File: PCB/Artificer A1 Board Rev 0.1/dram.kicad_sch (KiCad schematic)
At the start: 1 part, among them U4 K4F6E3S4HM-MGCJ

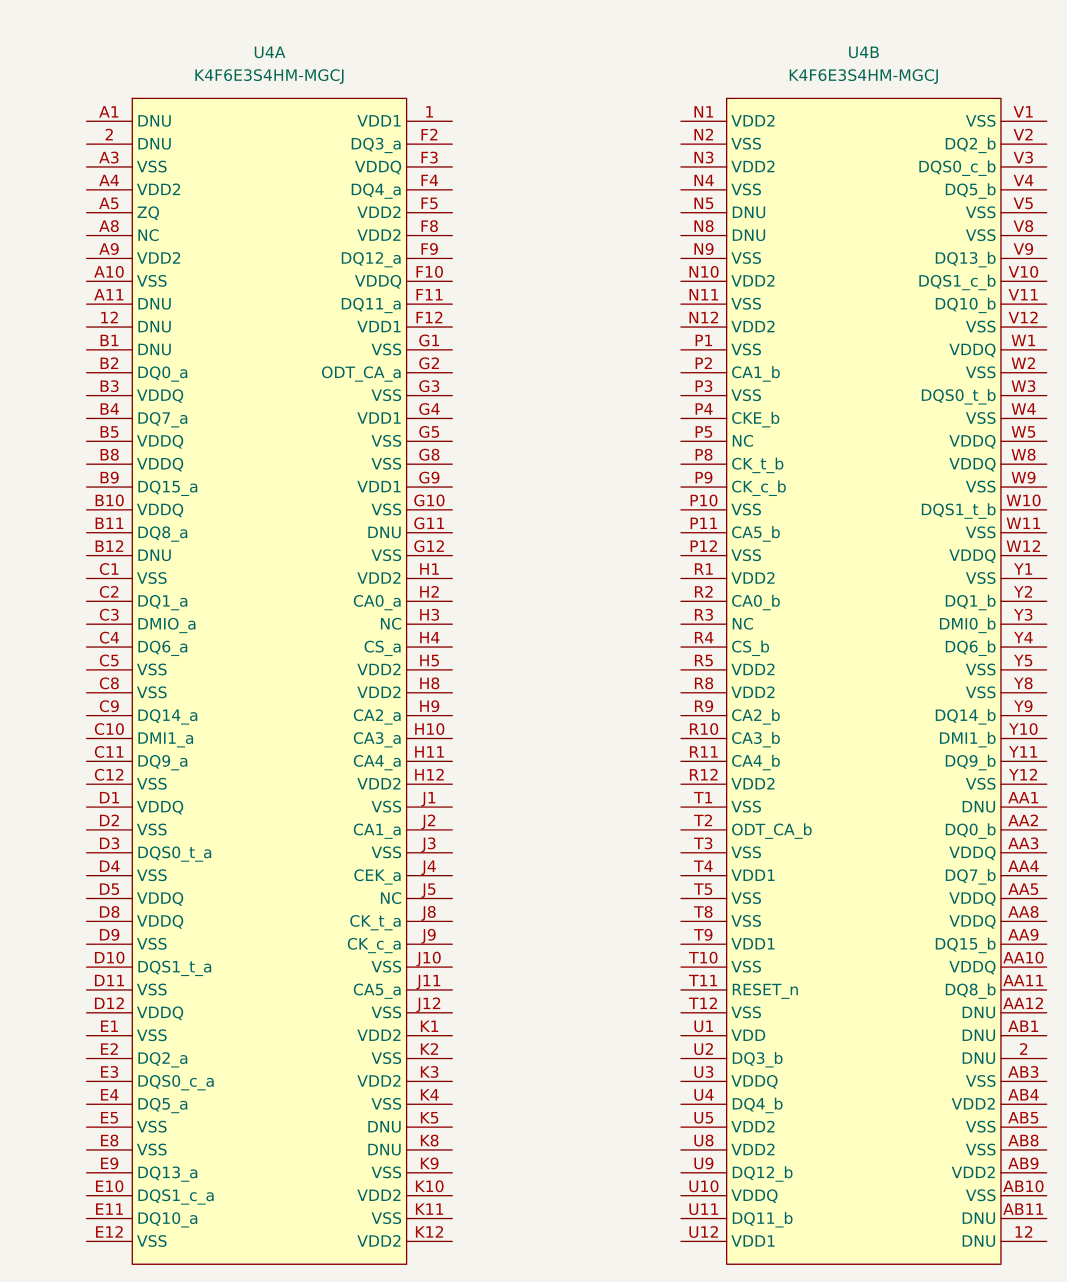
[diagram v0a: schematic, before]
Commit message: localized libraries
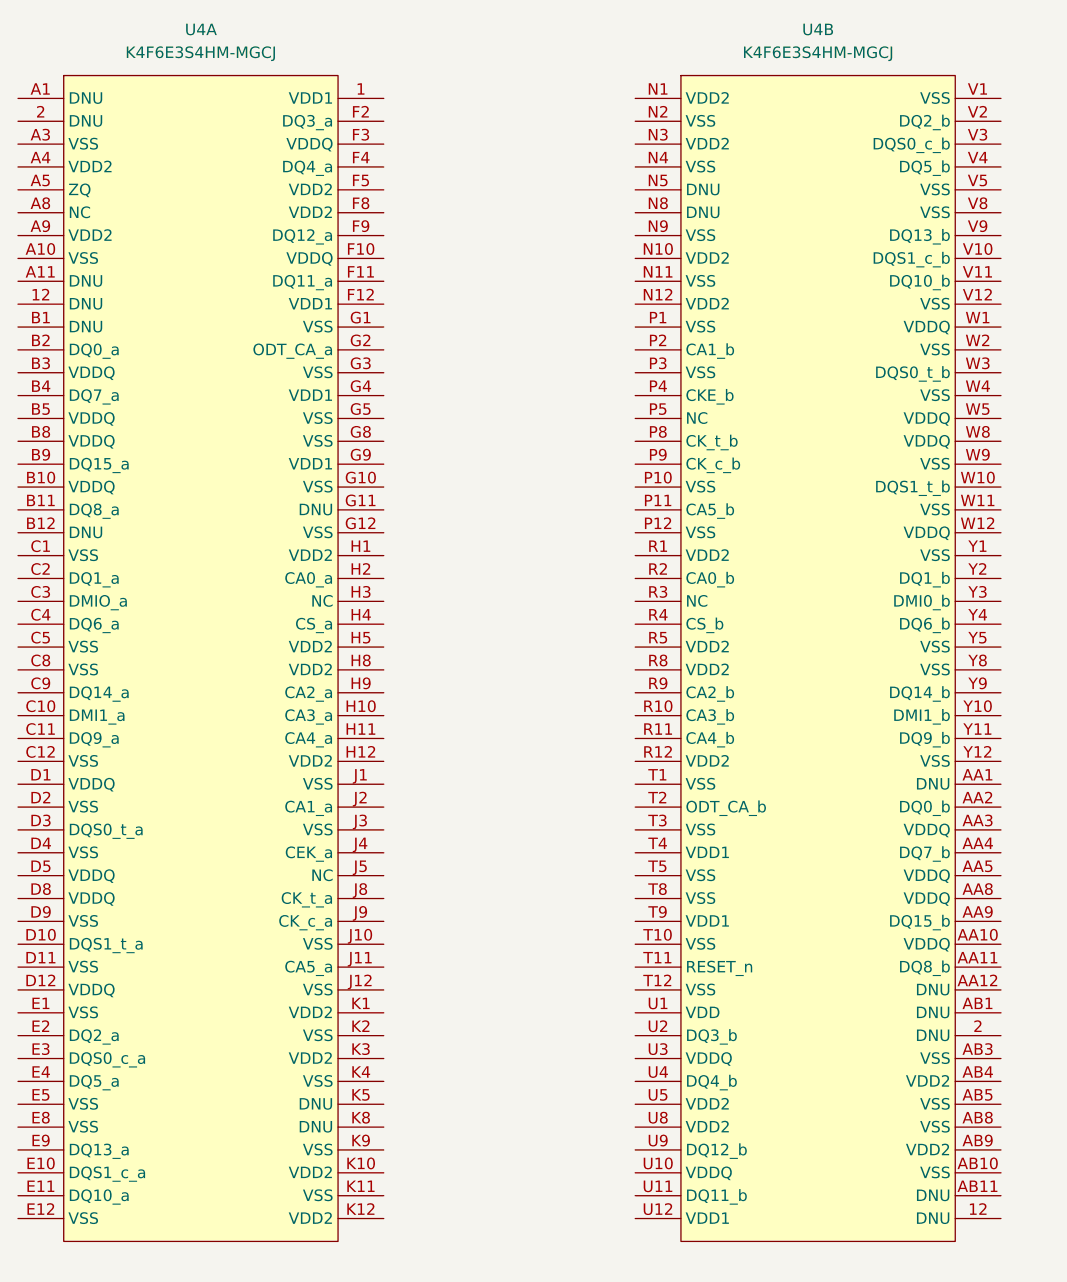
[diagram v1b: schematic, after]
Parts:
- removed U4: K4F6E3S4HM-MGCJ, easyeda2kicad:FBGA-200_L15.0-W10.0-BL_K4F6E3S4HM, symbol easyeda2kicad:K4F6E3S4HM-MGCJ
- added U4: K4F6E3S4HM-MGCJ, easyeda:FBGA-200_L15.0-W10.0-BL_K4F6E3S4HM, symbol easyeda:K4F6E3S4HM-MGCJ

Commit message: added a few accessories
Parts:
- removed U4: K4F6E3S4HM-MGCJ, easyeda:FBGA-200_L15.0-W10.0-BL_K4F6E3S4HM, symbol easyeda:K4F6E3S4HM-MGCJ
- added U14: K4UBE3D4AB-MGCL, easyeda:FBGA-200_L14.5-W10.0_RS1G32LF4D2BDS-53BT, symbol easyeda:K4UBE3D4AB-MGCL

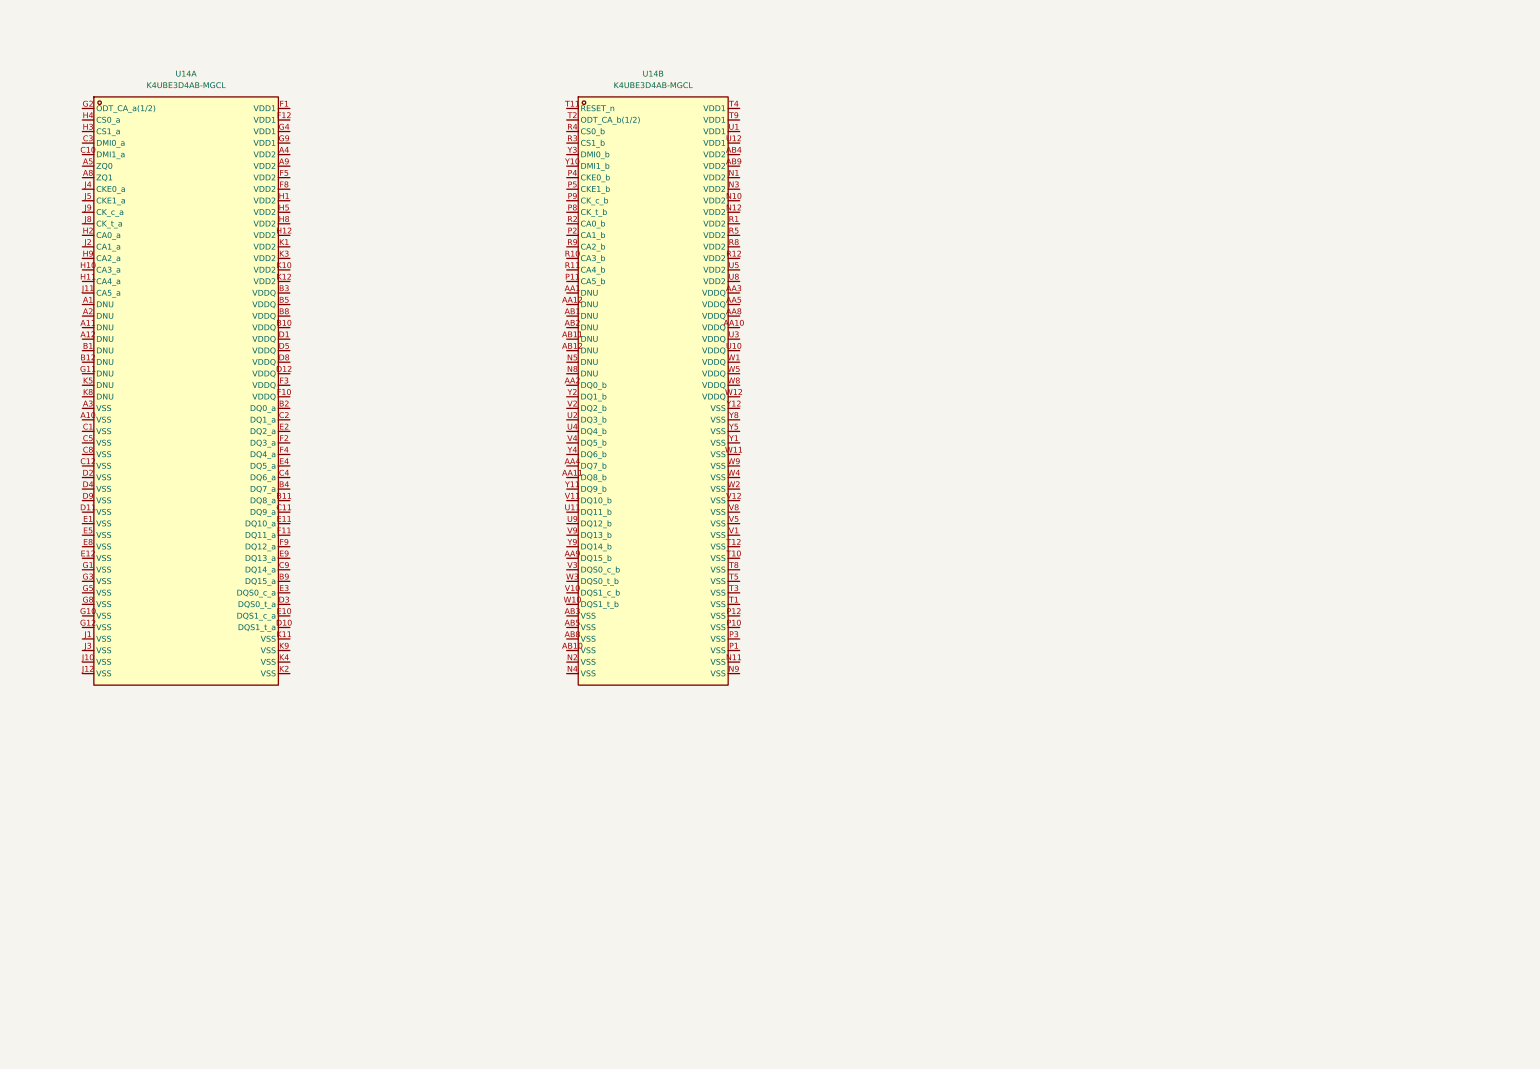
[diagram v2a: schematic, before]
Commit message: finished dram
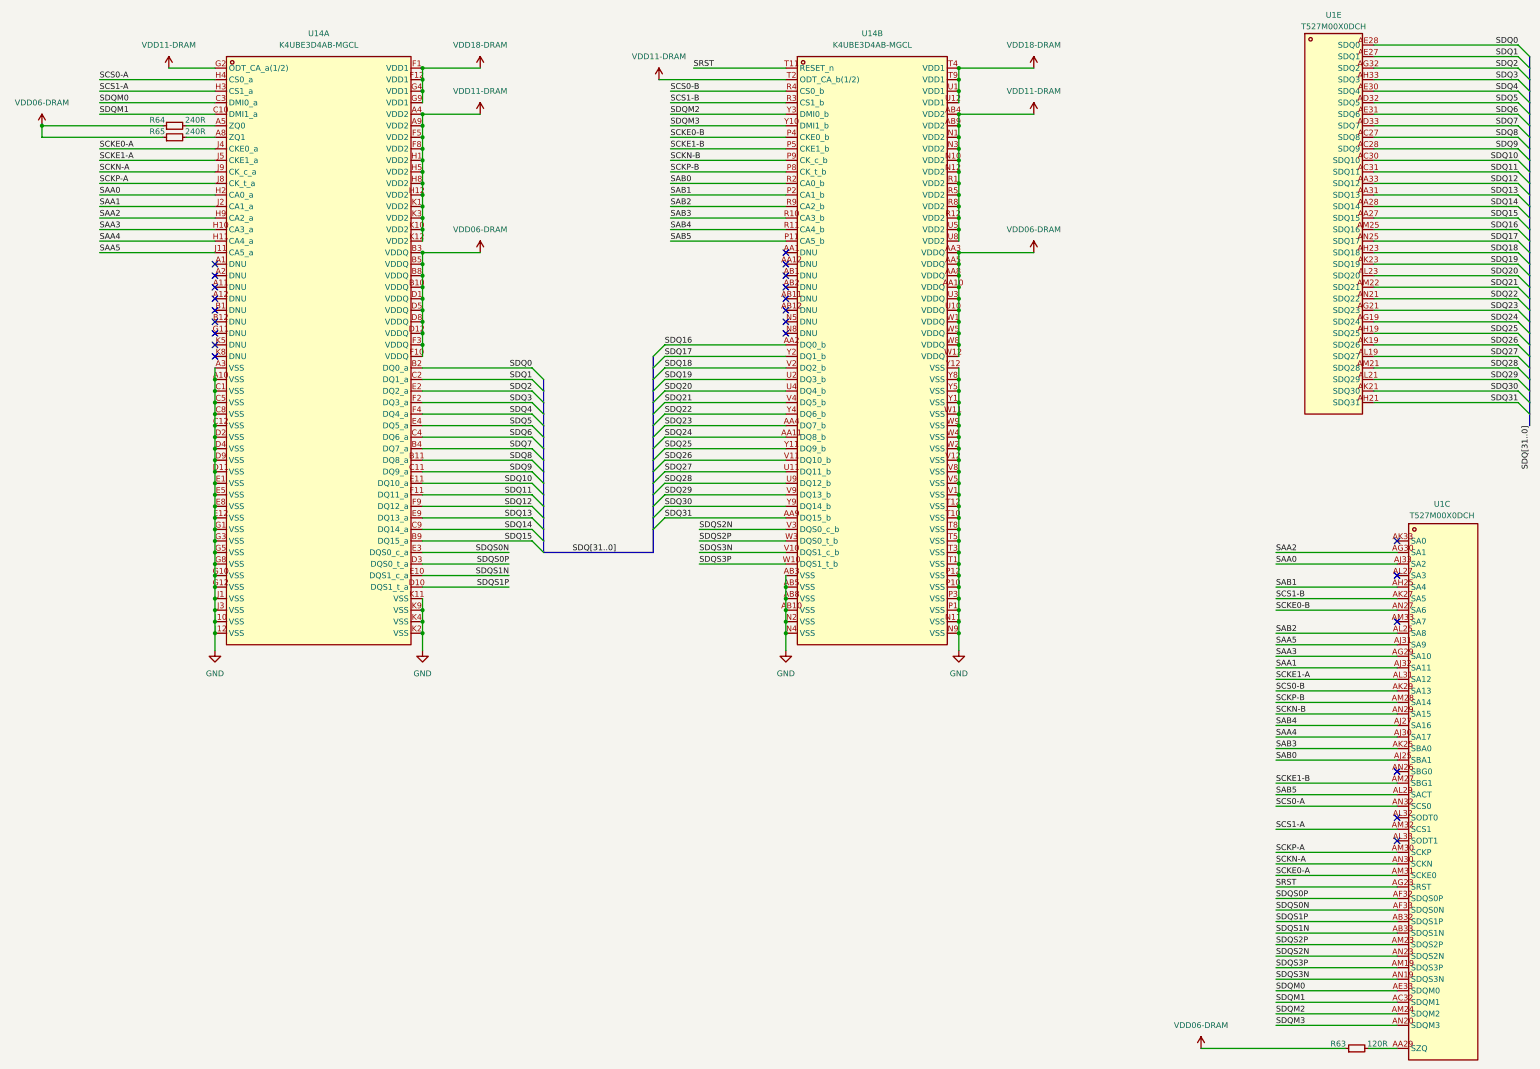
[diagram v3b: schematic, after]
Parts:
- added R63: 120R, symbol Device:R_Small
- added R64, R65: 240R, symbol Device:R_Small
- added U1: T527M00X0DCH, easyeda:BGA-664_L17.0-W17.0_T527, symbol easyeda:T527M00X0DCH
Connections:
- net GND: now reaches U14.A10 (VSS)
- net GND: now also U14.A3 (VSS), U14.AB10 (VSS), U14.AB3 (VSS), U14.AB5 (VSS), U14.AB8 (VSS), U14.C1 (VSS), U14.C12 (VSS), U14.C5 (VSS), U14.C8 (VSS), U14.D11 (VSS), U14.D2 (VSS), U14.D4 (VSS), U14.D9 (VSS), U14.E1 (VSS), U14.E12 (VSS), U14.E5 (VSS), U14.E8 (VSS), U14.G1 (VSS), U14.G10 (VSS), U14.G12 (VSS), U14.G3 (VSS), U14.G5 (VSS), U14.G8 (VSS), U14.J1 (VSS), U14.J10 (VSS), U14.J12 (VSS), U14.J3 (VSS), U14.K11 (VSS), U14.K2 (VSS), U14.K4 (VSS), U14.K9 (VSS), U14.N11 (VSS), U14.N2 (VSS), U14.N4 (VSS), U14.N9 (VSS), U14.P1 (VSS), U14.P10 (VSS), U14.P12 (VSS), U14.P3 (VSS), U14.T1 (VSS), U14.T10 (VSS), U14.T12 (VSS), U14.T3 (VSS), U14.T5 (VSS), U14.T8 (VSS), U14.V1 (VSS), U14.V12 (VSS), U14.V5 (VSS), U14.V8 (VSS), U14.W11 (VSS), U14.W2 (VSS), U14.W4 (VSS), U14.W9 (VSS), U14.Y1 (VSS), U14.Y12 (VSS), U14.Y5 (VSS), U14.Y8 (VSS)
- net VDD11-DRAM: now reaches U14.A4 (VDD2)
- net VDD11-DRAM: now also U14.A9 (VDD2), U14.AB4 (VDD2), U14.AB9 (VDD2), U14.F5 (VDD2), U14.F8 (VDD2), U14.G2 (ODT_CA_a(1/2)), U14.H1 (VDD2), U14.H12 (VDD2), U14.H5 (VDD2), U14.H8 (VDD2), U14.K1 (VDD2), U14.K10 (VDD2), U14.K12 (VDD2), U14.K3 (VDD2), U14.N1 (VDD2), U14.N10 (VDD2), U14.N12 (VDD2), U14.N3 (VDD2), U14.R1 (VDD2), U14.R12 (VDD2), U14.R5 (VDD2), U14.R8 (VDD2), U14.T2 (ODT_CA_b(1/2)), U14.U5 (VDD2), U14.U8 (VDD2)
- net at U14.A5 (ZQ0): now also R64.2
- net at U14.A8 (ZQ1): now also R65.2
- net VDD06-DRAM: now reaches U14.B10 (VDDQ)
- net VDD06-DRAM: now also U14.AA10 (VDDQ), U14.AA3 (VDDQ), U14.AA5 (VDDQ), U14.AA8 (VDDQ), U14.B3 (VDDQ), U14.B5 (VDDQ), U14.B8 (VDDQ), U14.D1 (VDDQ), U14.D12 (VDDQ), U14.D5 (VDDQ), U14.D8 (VDDQ), U14.F10 (VDDQ), U14.F3 (VDDQ), U14.U10 (VDDQ), U14.U3 (VDDQ), U14.W1 (VDDQ), U14.W12 (VDDQ), U14.W5 (VDDQ), U14.W8 (VDDQ), R63.1, R64.1, R65.1
- net SDQ8: now reaches U14.B11 (DQ8_a)
- net SDQ8: now also U1.AC27 (SDQ8)
- net SDQ0: now reaches U14.B2 (DQ0_a)
- net SDQ0: now also U1.AE28 (SDQ0)
- net SDQ7: now reaches U14.B4 (DQ7_a)
- net SDQ7: now also U1.AD33 (SDQ7)
- net SDQ15: now reaches U14.B9 (DQ15_a)
- net SDQ15: now also U1.AA27 (SDQ15)
- net SDQM1: now reaches U14.C10 (DMI1_a)
- net SDQM1: now also U1.AC32 (SDQM1)
- net SDQ9: now reaches U14.C11 (DQ9_a)
- net SDQ9: now also U1.AC28 (SDQ9)
- net SDQ1: now reaches U14.C2 (DQ1_a)
- net SDQ1: now also U1.AE27 (SDQ1)
- net SDQM0: now reaches U14.C3 (DMI0_a)
- net SDQM0: now also U1.AE33 (SDQM0)
- net SDQ6: now reaches U14.C4 (DQ6_a)
- net SDQ6: now also U1.AE31 (SDQ6)
- net SDQ14: now reaches U14.C9 (DQ14_a)
- net SDQ14: now also U1.AA28 (SDQ14)
- net SDQS1P: now reaches U14.D10 (DQS1_t_a)
- net SDQS1P: now also U1.AB32 (SDQS1P)
- net SDQS0P: now reaches U14.D3 (DQS0_t_a)
- net SDQS0P: now also U1.AF32 (SDQS0P)
- net SDQS1N: now reaches U14.E10 (DQS1_c_a)
- net SDQS1N: now also U1.AB33 (SDQS1N)
- net SDQ10: now reaches U14.E11 (DQ10_a)
- net SDQ10: now also U1.AC30 (SDQ10)
- net SDQ2: now reaches U14.E2 (DQ2_a)
- net SDQ2: now also U1.AG32 (SDQ2)
- net SDQS0N: now reaches U14.E3 (DQS0_c_a)
- net SDQS0N: now also U1.AF33 (SDQS0N)
- net SDQ5: now reaches U14.E4 (DQ5_a)
- net SDQ5: now also U1.AD32 (SDQ5)
- net SDQ13: now reaches U14.E9 (DQ13_a)
- net SDQ13: now also U1.AA31 (SDQ13)
- net VDD18-DRAM: now reaches U14.F1 (VDD1)
- net VDD18-DRAM: now also U14.F12 (VDD1), U14.G4 (VDD1), U14.G9 (VDD1), U14.T4 (VDD1), U14.T9 (VDD1), U14.U1 (VDD1), U14.U12 (VDD1)
- net SDQ11: now reaches U14.F11 (DQ11_a)
- net SDQ11: now also U1.AC31 (SDQ11)
- net SDQ3: now reaches U14.F2 (DQ3_a)
- net SDQ3: now also U1.AH33 (SDQ3)
- net SDQ4: now reaches U14.F4 (DQ4_a)
- net SDQ4: now also U1.AE30 (SDQ4)
- net SDQ12: now reaches U14.F9 (DQ12_a)
- net SDQ12: now also U1.AA33 (SDQ12)
- net SAA3: now reaches U14.H10 (CA3_a)
- net SAA3: now also U1.AG29 (SA10)
- net SAA4: now reaches U14.H11 (CA4_a)
- net SAA4: now also U1.AJ30 (SA17)
- net SAA0: now reaches U14.H2 (CA0_a)
- net SAA0: now also U1.AJ33 (SA2)
- net SCS1-A: now reaches U14.H3 (CS1_a)
- net SCS1-A: now also U1.AM32 (SCS1)
- net SCS0-A: now reaches U14.H4 (CS0_a)
- net SCS0-A: now also U1.AN32 (SCS0)
- net SAA2: now reaches U14.H9 (CA2_a)
- net SAA2: now also U1.AG30 (SA1)
- net SAA5: now reaches U14.J11 (CA5_a)
- net SAA5: now also U1.AJ31 (SA9)
- net SAA1: now reaches U14.J2 (CA1_a)
- net SAA1: now also U1.AJ32 (SA11)
- net SCKE0-A: now reaches U14.J4 (CKE0_a)
- net SCKE0-A: now also U1.AM31 (SCKE0)
- net SCKE1-A: now reaches U14.J5 (CKE1_a)
- net SCKE1-A: now also U1.AL31 (SA12)
- net SCKP-A: now reaches U14.J8 (CK_t_a)
- net SCKP-A: now also U1.AM30 (SCKP)
- net SCKN-A: now reaches U14.J9 (CK_c_a)
- net SCKN-A: now also U1.AN30 (SCKN)
- net SDQ24: now reaches U14.AA11 (DQ8_b)
- net SDQ24: now also U1.AG19 (SDQ24)
- net SDQ16: now reaches U14.AA2 (DQ0_b)
- net SDQ16: now also U1.AM25 (SDQ16)
- net SDQ23: now reaches U14.AA4 (DQ7_b)
- net SDQ23: now also U1.AG21 (SDQ23)
- net SDQ31: now reaches U14.AA9 (DQ15_b)
- net SDQ31: now also U1.AH21 (SDQ31)
- net SAB5: now reaches U14.P11 (CA5_b)
- net SAB5: now also U1.AL29 (SACT)
- net SAB1: now reaches U14.P2 (CA1_b)
- net SAB1: now also U1.AH25 (SA4)
- net SCKE0-B: now reaches U14.P4 (CKE0_b)
- net SCKE0-B: now also U1.AN27 (SA6)
- net SCKE1-B: now reaches U14.P5 (CKE1_b)
- net SCKE1-B: now also U1.AM27 (SBG1)
- net SCKP-B: now reaches U14.P8 (CK_t_b)
- net SCKP-B: now also U1.AM28 (SA14)
- net SCKN-B: now reaches U14.P9 (CK_c_b)
- net SCKN-B: now also U1.AN29 (SA15)
- net SAB3: now reaches U14.R10 (CA3_b)
- net SAB3: now also U1.AK25 (SBA0)
- net SAB4: now reaches U14.R11 (CA4_b)
- net SAB4: now also U1.AJ27 (SA16)
- net SAB0: now reaches U14.R2 (CA0_b)
- net SAB0: now also U1.AJ25 (SBA1)
- net SCS1-B: now reaches U14.R3 (CS1_b)
- net SCS1-B: now also U1.AK27 (SA5)
- net SCS0-B: now reaches U14.R4 (CS0_b)
- net SCS0-B: now also U1.AK29 (SA13)
- net SAB2: now reaches U14.R9 (CA2_b)
- net SAB2: now also U1.AL25 (SA8)
- net SRST: now reaches U14.T11 (RESET_n)
- net SRST: now also U1.AG23 (SRST)
- net SDQ27: now reaches U14.U11 (DQ11_b)
- net SDQ27: now also U1.AL19 (SDQ27)
- net SDQ19: now reaches U14.U2 (DQ3_b)
- net SDQ19: now also U1.AK23 (SDQ19)
- net SDQ20: now reaches U14.U4 (DQ4_b)
- net SDQ20: now also U1.AL23 (SDQ20)
- net SDQ28: now reaches U14.U9 (DQ12_b)
- net SDQ28: now also U1.AM21 (SDQ28)
- net SDQS3N: now reaches U14.V10 (DQS1_c_b)
- net SDQS3N: now also U1.AN19 (SDQS3N)
- net SDQ26: now reaches U14.V11 (DQ10_b)
- net SDQ26: now also U1.AK19 (SDQ26)
- net SDQ18: now reaches U14.V2 (DQ2_b)
- net SDQ18: now also U1.AH23 (SDQ18)
- net SDQS2N: now reaches U14.V3 (DQS0_c_b)
- net SDQS2N: now also U1.AN23 (SDQS2N)
- net SDQ21: now reaches U14.V4 (DQ5_b)
- net SDQ21: now also U1.AM22 (SDQ21)
- net SDQ29: now reaches U14.V9 (DQ13_b)
- net SDQ29: now also U1.AL21 (SDQ29)
- net SDQS3P: now reaches U14.W10 (DQS1_t_b)
- net SDQS3P: now also U1.AM19 (SDQS3P)
- net SDQS2P: now reaches U14.W3 (DQS0_t_b)
- net SDQS2P: now also U1.AM23 (SDQS2P)
- net SDQM3: now reaches U14.Y10 (DMI1_b)
- net SDQM3: now also U1.AN20 (SDQM3)
- net SDQ25: now reaches U14.Y11 (DQ9_b)
- net SDQ25: now also U1.AH19 (SDQ25)
- net SDQ17: now reaches U14.Y2 (DQ1_b)
- net SDQ17: now also U1.AN25 (SDQ17)
- net SDQM2: now reaches U14.Y3 (DMI0_b)
- net SDQM2: now also U1.AM24 (SDQM2)
- net SDQ22: now reaches U14.Y4 (DQ6_b)
- net SDQ22: now also U1.AN21 (SDQ22)
- net SDQ30: now reaches U14.Y9 (DQ14_b)
- net SDQ30: now also U1.AK21 (SDQ30)
- new net: R63.2, U1.AA29 (SZQ)
- no-connect marks 0 -> 23
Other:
- moved on the sheet: U14A, U14B

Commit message: added features
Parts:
- removed unit 3 of U1
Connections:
- net SAA0: now also U1.AJ33 (SA2)
- net SAA1: now also U1.AJ32 (SA11)
- net SAA2: now also U1.AG30 (SA1)
- net SAA3: now also U1.AG29 (SA10)
- net SAA4: now also U1.AJ30 (SA17)
- net SAA5: now also U1.AJ31 (SA9)
- net SAB0: now also U1.AJ25 (SBA1)
- net SAB1: now also U1.AH25 (SA4)
- net SAB2: now also U1.AL25 (SA8)
- net SAB3: now also U1.AK25 (SBA0)
- net SAB4: now also U1.AJ27 (SA16)
- net SAB5: now also U1.AL29 (SACT)
- net SCKE0-A: now also U1.AM31 (SCKE0)
- net SCKE0-B: now also U1.AN27 (SA6)
- net SCKE1-A: now also U1.AL31 (SA12)
- net SCKE1-B: now also U1.AM27 (SBG1)
- net SCKN-A: now also U1.AN30 (SCKN)
- net SCKN-B: now also U1.AN29 (SA15)
- net SCKP-A: now also U1.AM30 (SCKP)
- net SCKP-B: now also U1.AM28 (SA14)
- net SCS0-A: now also U1.AN32 (SCS0)
- net SCS0-B: now also U1.AK29 (SA13)
- net SCS1-A: now also U1.AM32 (SCS1)
- net SCS1-B: now also U1.AK27 (SA5)
- net SDQM0: now also U1.AE33 (SDQM0)
- net SDQM1: now also U1.AC32 (SDQM1)
- net SDQM2: now also U1.AM24 (SDQM2)
- net SDQM3: now also U1.AN20 (SDQM3)
- net SDQS0N: now also U1.AF33 (SDQS0N)
- net SDQS0P: now also U1.AF32 (SDQS0P)
- net SDQS1N: now also U1.AB33 (SDQS1N)
- net SDQS1P: now also U1.AB32 (SDQS1P)
- net SDQS2N: now also U1.AN23 (SDQS2N)
- net SDQS2P: now also U1.AM23 (SDQS2P)
- net SDQS3N: now also U1.AN19 (SDQS3N)
- net SDQS3P: now also U1.AM19 (SDQS3P)
- net SRST: now also U1.AG23 (SRST)
- net VDD06-DRAM: now also U1.AC17 (VCCDRAML), U1.AC18 (VCCDRAML), U1.AC19 (VCCDRAML), U1.AC20 (VCCDRAML), U1.AC22 (VCCDRAML)
- net VDD11-DRAM: now also U1.AA24 (VCCDRAM), U1.AB24 (VCCDRAM), U1.AC24 (VCCDRAM), U1.W23 (VCCDRAM), U1.W24 (VCCDRAM), U1.W25 (VCCDRAM), U1.Y24 (VCCDRAM)
- net VDD18-DRAM: now also U1.AD25 (VDD18-DRAM)
- net at R63.2: now also U1.AA29 (SZQ)
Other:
- note added: "LPDDR4X"
- moved on the sheet: R63, R64, R65, U14A, U14B
